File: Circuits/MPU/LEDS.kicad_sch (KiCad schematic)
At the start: 0 parts

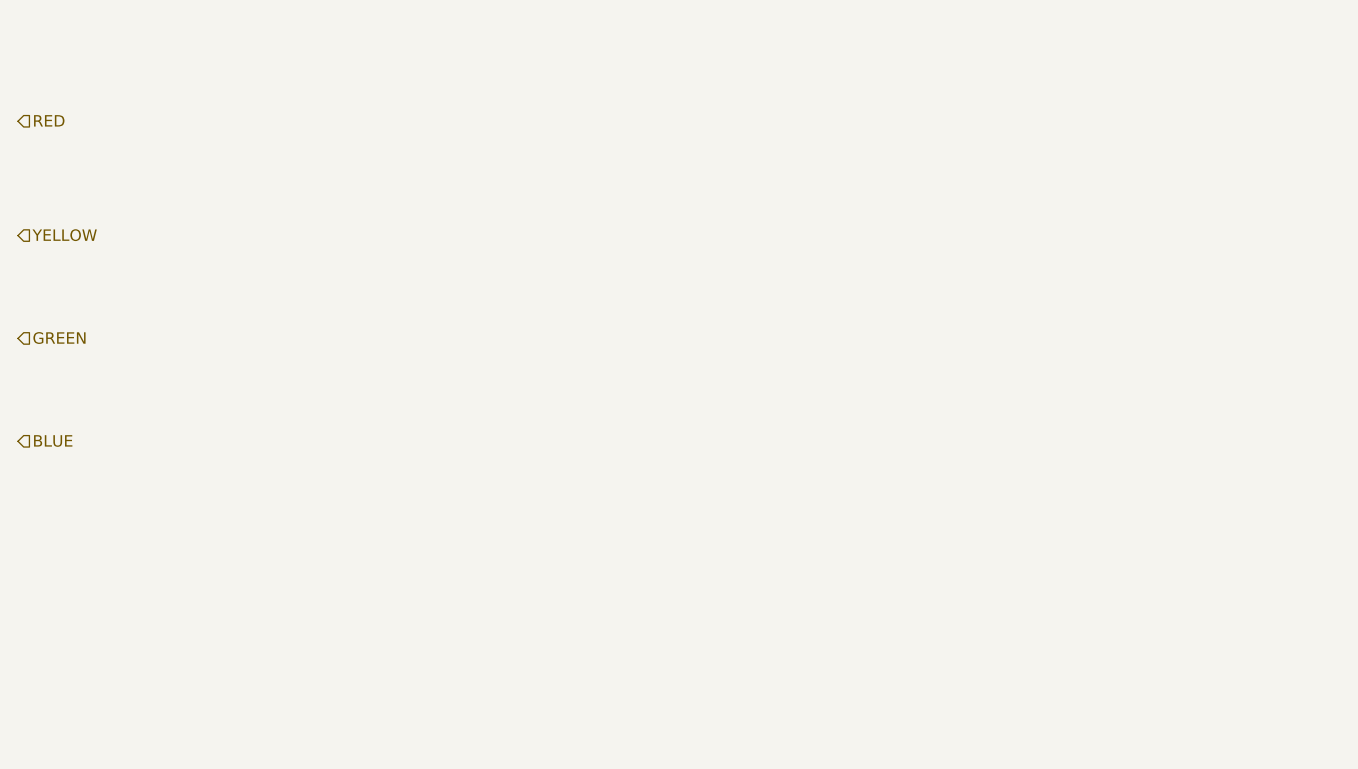
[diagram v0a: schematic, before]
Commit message: All pages populated with parts
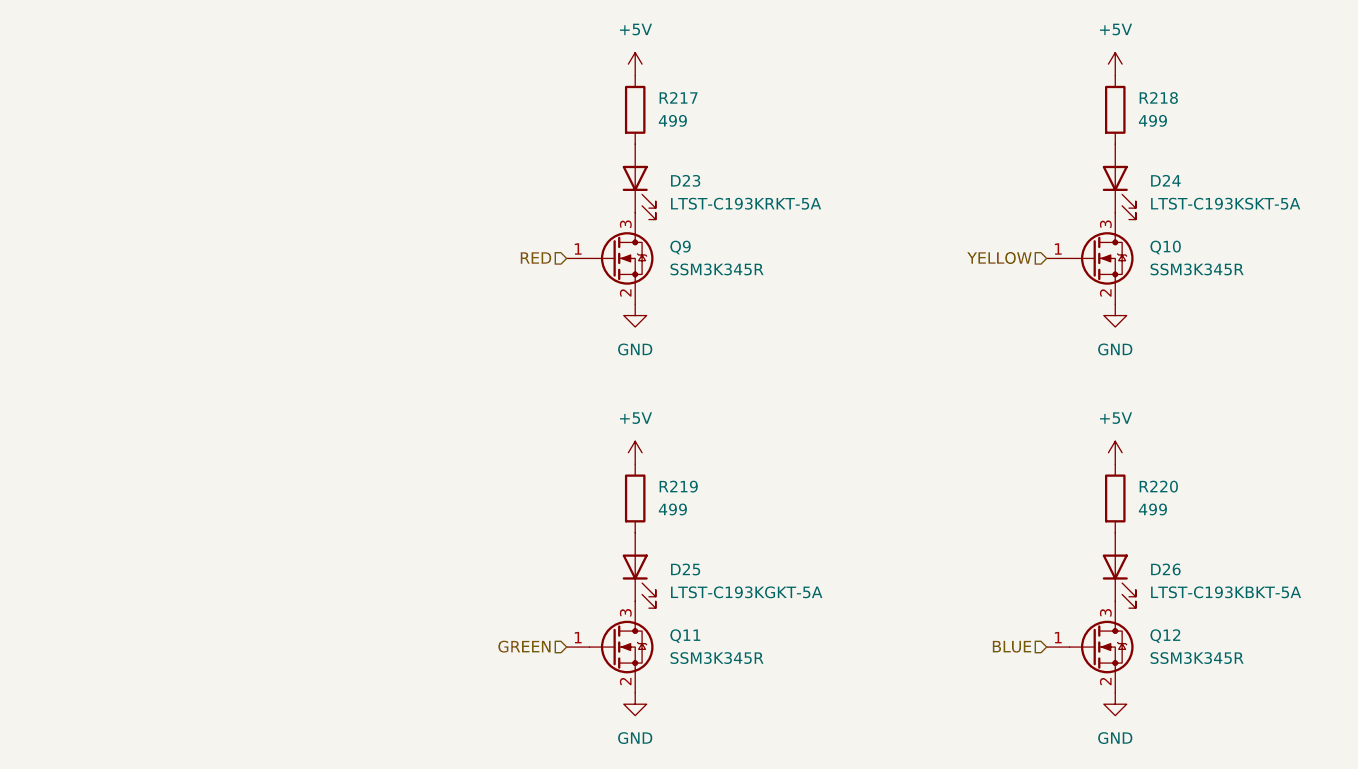
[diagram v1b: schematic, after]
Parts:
- added D23: LTST-C193KRKT-5A, LED_SMD:LED_0603_1608Metric, symbol LED:IR26-21C_L110_TR8
- added D24: LTST-C193KSKT-5A, LED_SMD:LED_0603_1608Metric, symbol LED:IR26-21C_L110_TR8
- added D25: LTST-C193KGKT-5A, LED_SMD:LED_0603_1608Metric, symbol LED:IR26-21C_L110_TR8
- added D26: LTST-C193KBKT-5A, LED_SMD:LED_0603_1608Metric, symbol LED:IR26-21C_L110_TR8
- added Q10, Q11, Q12, Q9: SSM3K345R, Package_TO_SOT_SMD:SOT-23, symbol QuERI_symbols:SSM3K345R
- added R217, R218, R219, R220: 499, Resistor_SMD:R_0603_1608Metric, symbol QuERI_symbols:Rlowp
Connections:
- net BLUE: now also Q12.1 (G)
- net GREEN: now also Q11.1 (G)
- net RED: now also Q9.1 (G)
- net YELLOW: now also Q10.1 (G)
- new net: D26.2 (A), R220.2
- new net: D26.1 (K), Q12.3 (D)
- new net: D24.1 (K), Q10.3 (D)
- new net: D25.1 (K), Q11.3 (D)
- new net: D25.2 (A), R219.2
- new net: D23.1 (K), Q9.3 (D)
- new net: D23.2 (A), R217.2
- new net: D24.2 (A), R218.2
- new net +5V: R217.1, R218.1, R219.1, R220.1
- new net GND: Q10.2 (S), Q11.2 (S), Q12.2 (S), Q9.2 (S)

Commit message: Passes DRC
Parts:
- renumbered D23 to D15, D25 to D16, D24 to D17, D26 to D18, Q11 to Q10, Q10 to Q11, R217 to R101, R219 to R102, R218 to R103, R220 to R104
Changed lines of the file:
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@@
 		(dnp no)
 		(fields_autoplaced yes)
-		(property "Reference" "#PWR0320"
+		(property "Reference" "#PWR0174"
 			(at 118.11 87.63 0)
 			(effects
@@
 			(project "MPU"
 				(path "/a3d8c1ad-4320-4fce-bd93-27782a1083f9/028dc115-76c0-407b-8cb2-dbe1c892e7d7"
-					(reference "#PWR0320")
+					(reference "#PWR0174")
 					(unit 1)
 				)
@@
 		(dnp no)
 		(fields_autoplaced yes)
-		(property "Reference" "R220"
+		(property "Reference" "R104"
 			(at 173.99 86.3599 0)
 			(effects
@@
 			(project "MPU"
 				(path "/a3d8c1ad-4320-4fce-bd93-27782a1083f9/028dc115-76c0-407b-8cb2-dbe1c892e7d7"
-					(reference "R220")
+					(reference "R104")
 					(unit 1)
 				)
@@
 		(dnp no)
 		(fields_autoplaced yes)
-		(property "Reference" "D26"
+		(property "Reference" "D18"
 			(at 175.26 95.5674 90)
 			(effects
@@
 			)
 		)
-		(property "Datasheet" "https://optoelectronics.liteon.com/upload/download/DS22-2005-077/LTST-C193KRKT-5A.PDF"
+		(property "Datasheet" "http://www.everlight.com/file/ProductFile/IR26-21C-L110-TR8.pdf"
 			(at 171.45 95.25 0)
 			(effects
@@
 			)
 		)
-		(property "Description" "BLUE LED"
+		(property "Description" "940nm, 20 deg, Infrared LED, 1206"
 			(at 171.45 95.25 0)
 			(effects
@@
 			(project "MPU"
 				(path "/a3d8c1ad-4320-4fce-bd93-27782a1083f9/028dc115-76c0-407b-8cb2-dbe1c892e7d7"
-					(reference "D26")
+					(reference "D18")
 					(unit 1)
 				)
@@
 		(dnp no)
 		(fields_autoplaced yes)
-		(property "Reference" "#PWR0316"
+		(property "Reference" "#PWR0172"
 			(at 118.11 44.45 0)
 			(effects
@@
 			(project "MPU"
 				(path "/a3d8c1ad-4320-4fce-bd93-27782a1083f9/028dc115-76c0-407b-8cb2-dbe1c892e7d7"
-					(reference "#PWR0316")
+					(reference "#PWR0172")
 					(unit 1)
 				)
@@
 		(dnp no)
 		(fields_autoplaced yes)
-		(property "Reference" "#PWR0319"
+		(property "Reference" "#PWR0177"
 			(at 171.45 72.39 0)
 			(effects
@@
 			(project "MPU"
 				(path "/a3d8c1ad-4320-4fce-bd93-27782a1083f9/028dc115-76c0-407b-8cb2-dbe1c892e7d7"
-					(reference "#PWR0319")
+					(reference "#PWR0177")
 					(unit 1)
 				)
@@
 		(dnp no)
 		(fields_autoplaced yes)
-		(property "Reference" "#PWR0323"
+		(property "Reference" "#PWR0179"
 			(at 171.45 115.57 0)
 			(effects
@@
 			(project "MPU"
 				(path "/a3d8c1ad-4320-4fce-bd93-27782a1083f9/028dc115-76c0-407b-8cb2-dbe1c892e7d7"
-					(reference "#PWR0323")
+					(reference "#PWR0179")
 					(unit 1)
 				)
@@
 		(dnp no)
 		(fields_autoplaced yes)
-		(property "Reference" "Q10"
+		(property "Reference" "Q11"
 			(at 175.26 59.6899 0)
 			(effects
@@
 			(project "MPU"
 				(path "/a3d8c1ad-4320-4fce-bd93-27782a1083f9/028dc115-76c0-407b-8cb2-dbe1c892e7d7"
-					(reference "Q10")
+					(reference "Q11")
 					(unit 1)
 				)
@@
 		(dnp no)
 		(fields_autoplaced yes)
-		(property "Reference" "#PWR0322"
+		(property "Reference" "#PWR0178"
 			(at 171.45 87.63 0)
 			(effects
@@
 			(project "MPU"
 				(path "/a3d8c1ad-4320-4fce-bd93-27782a1083f9/028dc115-76c0-407b-8cb2-dbe1c892e7d7"
-					(reference "#PWR0322")
+					(reference "#PWR0178")
 					(unit 1)
 				)
@@
 		(dnp no)
 		(fields_autoplaced yes)
-		(property "Reference" "D25"
+		(property "Reference" "D16"
 			(at 121.92 95.5674 90)
 			(effects
@@
 			)
 		)
-		(property "Datasheet" "https://optoelectronics.liteon.com/upload/download/DS22-2005-077/LTST-C193KRKT-5A.PDF"
+		(property "Datasheet" "http://www.everlight.com/file/ProductFile/IR26-21C-L110-TR8.pdf"
 			(at 118.11 95.25 0)
 			(effects
@@
 			)
 		)
-		(property "Description" "GREEN LED"
+		(property "Description" "940nm, 20 deg, Infrared LED, 1206"
 			(at 118.11 95.25 0)
 			(effects
@@
 			(project "MPU"
 				(path "/a3d8c1ad-4320-4fce-bd93-27782a1083f9/028dc115-76c0-407b-8cb2-dbe1c892e7d7"
-					(reference "D25")
+					(reference "D16")
 					(unit 1)
 				)
@@
 		(dnp no)
 		(fields_autoplaced yes)
-		(property "Reference" "#PWR0317"
+		(property "Reference" "#PWR0173"
 			(at 118.11 72.39 0)
 			(effects
@@
 			(project "MPU"
 				(path "/a3d8c1ad-4320-4fce-bd93-27782a1083f9/028dc115-76c0-407b-8cb2-dbe1c892e7d7"
-					(reference "#PWR0317")
+					(reference "#PWR0173")
 					(unit 1)
 				)
@@
 		(dnp no)
 		(fields_autoplaced yes)
-		(property "Reference" "#PWR0321"
+		(property "Reference" "#PWR0175"
 			(at 118.11 115.57 0)
 			(effects
@@
 			(project "MPU"
 				(path "/a3d8c1ad-4320-4fce-bd93-27782a1083f9/028dc115-76c0-407b-8cb2-dbe1c892e7d7"
-					(reference "#PWR0321")
+					(reference "#PWR0175")
 					(unit 1)
 				)
@@
 		(dnp no)
 		(fields_autoplaced yes)
-		(property "Reference" "D23"
+		(property "Reference" "D15"
 			(at 121.92 52.3874 90)
 			(effects
@@
 			)
 		)
-		(property "Datasheet" "https://optoelectronics.liteon.com/upload/download/DS22-2005-077/LTST-C193KRKT-5A.PDF"
+		(property "Datasheet" "http://www.everlight.com/file/ProductFile/IR26-21C-L110-TR8.pdf"
 			(at 118.11 52.07 0)
 			(effects
@@
 			)
 		)
-		(property "Description" "RED LED"
+		(property "Description" "940nm, 20 deg, Infrared LED, 1206"
 			(at 118.11 52.07 0)
 			(effects
@@
 			(project "MPU"
 				(path "/a3d8c1ad-4320-4fce-bd93-27782a1083f9/028dc115-76c0-407b-8cb2-dbe1c892e7d7"
-					(reference "D23")
+					(reference "D15")
 					(unit 1)
 				)
@@
 		(dnp no)
 		(fields_autoplaced yes)
-		(property "Reference" "R219"
+		(property "Reference" "R102"
 			(at 120.65 86.3599 0)
 			(effects
@@
 			(project "MPU"
 				(path "/a3d8c1ad-4320-4fce-bd93-27782a1083f9/028dc115-76c0-407b-8cb2-dbe1c892e7d7"
-					(reference "R219")
+					(reference "R102")
 					(unit 1)
 				)
@@
 		(dnp no)
 		(fields_autoplaced yes)
-		(property "Reference" "#PWR0318"
+		(property "Reference" "#PWR0176"
 			(at 171.45 44.45 0)
 			(effects
@@
 			(project "MPU"
 				(path "/a3d8c1ad-4320-4fce-bd93-27782a1083f9/028dc115-76c0-407b-8cb2-dbe1c892e7d7"
-					(reference "#PWR0318")
+					(reference "#PWR0176")
 					(unit 1)
 				)
@@
 		(dnp no)
 		(fields_autoplaced yes)
-		(property "Reference" "R218"
+		(property "Reference" "R103"
 			(at 173.99 43.1799 0)
 			(effects
@@
 			(project "MPU"
 				(path "/a3d8c1ad-4320-4fce-bd93-27782a1083f9/028dc115-76c0-407b-8cb2-dbe1c892e7d7"
-					(reference "R218")
+					(reference "R103")
 					(unit 1)
 				)
@@
 		(dnp no)
 		(fields_autoplaced yes)
-		(property "Reference" "D24"
+		(property "Reference" "D17"
 			(at 175.26 52.3874 90)
 			(effects
@@
 			)
 		)
-		(property "Datasheet" "https://optoelectronics.liteon.com/upload/download/DS22-2005-077/LTST-C193KRKT-5A.PDF"
+		(property "Datasheet" "http://www.everlight.com/file/ProductFile/IR26-21C-L110-TR8.pdf"
 			(at 171.45 52.07 0)
 			(effects
@@
 			)
 		)
-		(property "Description" "YELLOW LED"
+		(property "Description" "940nm, 20 deg, Infrared LED, 1206"
 			(at 171.45 52.07 0)
 			(effects
@@
 			(project "MPU"
 				(path "/a3d8c1ad-4320-4fce-bd93-27782a1083f9/028dc115-76c0-407b-8cb2-dbe1c892e7d7"
-					(reference "D24")
+					(reference "D17")
 					(unit 1)
 				)
@@
 		(dnp no)
 		(fields_autoplaced yes)
-		(property "Reference" "R217"
+		(property "Reference" "R101"
 			(at 120.65 43.1799 0)
 			(effects
@@
 			(project "MPU"
 				(path "/a3d8c1ad-4320-4fce-bd93-27782a1083f9/028dc115-76c0-407b-8cb2-dbe1c892e7d7"
-					(reference "R217")
+					(reference "R101")
 					(unit 1)
 				)
@@
 		(dnp no)
 		(fields_autoplaced yes)
-		(property "Reference" "Q11"
+		(property "Reference" "Q10"
 			(at 121.92 102.8699 0)
 			(effects
@@
 			(project "MPU"
 				(path "/a3d8c1ad-4320-4fce-bd93-27782a1083f9/028dc115-76c0-407b-8cb2-dbe1c892e7d7"
-					(reference "Q11")
-					(unit 1)
-				)
+					(reference "Q10")
+					(unit 1)
+				)
